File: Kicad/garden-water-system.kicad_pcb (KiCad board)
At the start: 2 copper layers, 75 x 60 mm, 36 parts, among them J1 Conn_01x02, J10 Screw_Terminal_01x05, J11 Conn_01x04, J12 Conn_01x05, J13 Jack-DC, J2 Conn_01x05, J3 Conn_01x03, J4 Conn_01x03, J5 Conn_01x03, J6 Conn_01x03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

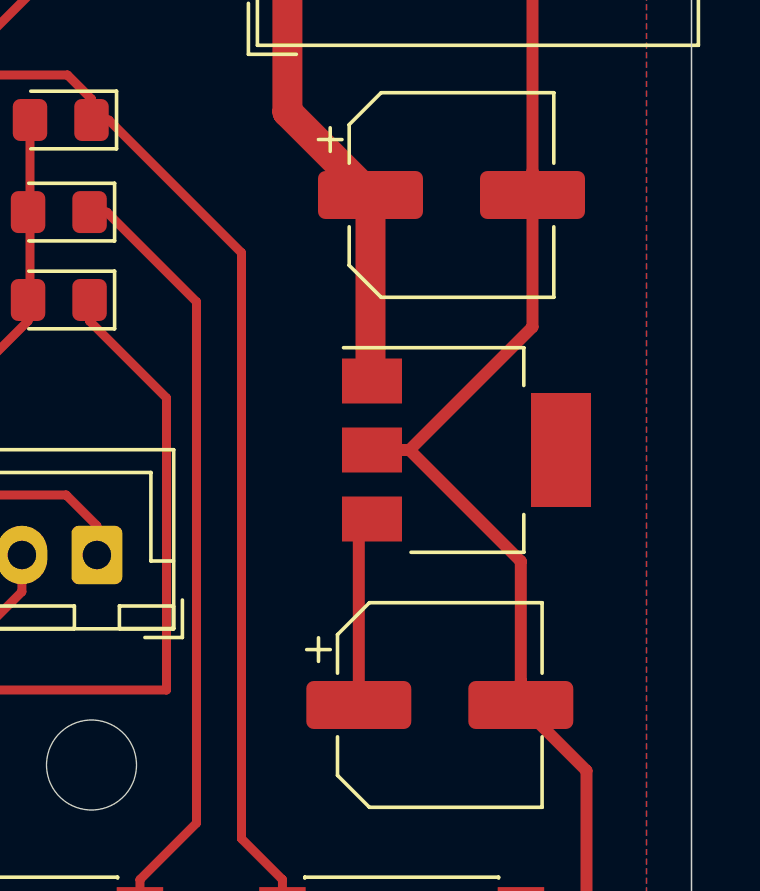
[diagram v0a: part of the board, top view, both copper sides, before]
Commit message: Correction pins AMS1117 5.0
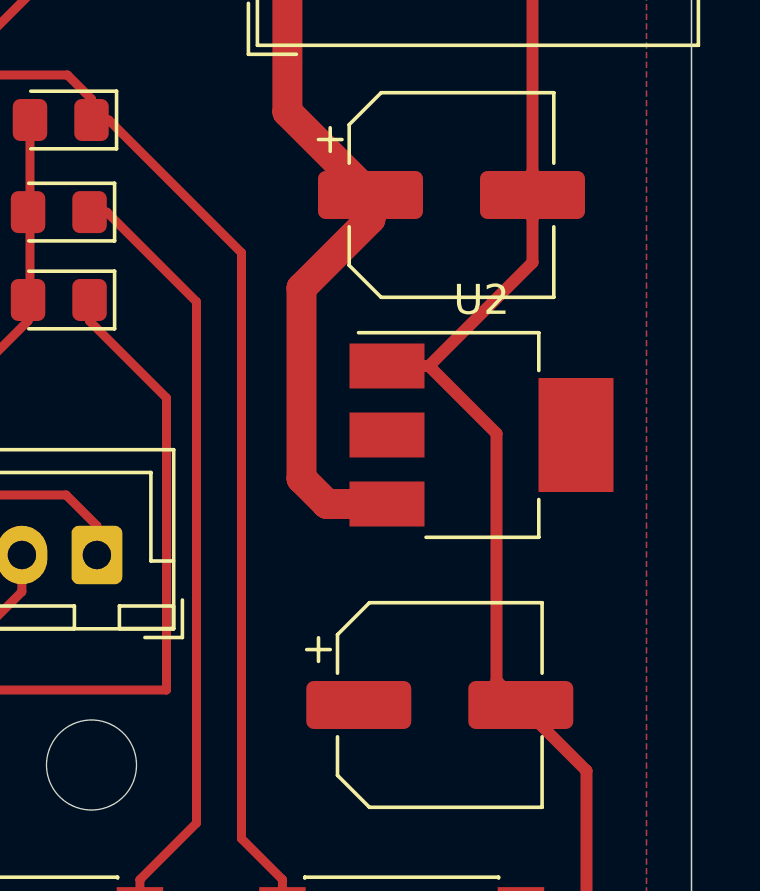
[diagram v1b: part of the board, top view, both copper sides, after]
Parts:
- U2: value LM7805_TO220 -> AMS1117-5.0
- moved U2 0.71 mm to (183.0, 59.5)
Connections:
- U2 pad 1: Net-(C4-Pad1) -> GND
- U2 pad 2: GND -> VCC
- U2 pad 3: VCC -> Net-(C4-Pad1)
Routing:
- net Net-(C4-Pad1): track 23.1 -> 30.5 mm
- net VCC: track 6.38 -> 0.00 mm
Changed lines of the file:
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@@
     (thickness 1.6)
     (drawings 12)
-    (tracks 202)
+    (tracks 204)
     (zones 0)
     (modules 36)
@@
     (mod_text_size 1 1)
     (mod_text_width 0.15)
-    (pad_size 3 3)
-    (pad_drill 3)
+    (pad_size 2.5 3.8)
+    (pad_drill 0)
     (pad_to_mask_clearance 0.051)
     (solder_mask_min_width 0.25)
@@
     (uvia_drill 0.1)
     (add_net VCC)
+  )
+  (module Package_TO_SOT_SMD:SOT-223 (layer F.Cu)
+    (at 183 59.5)
+    (descr "module CMS SOT223 4 pins")
+    (tags "CMS SOT")
+    (attr smd)
+    (fp_text reference U2 (at 0 -4.5) (layer F.SilkS)
+      (effects (font (size 1 1) (thickness 0.15)))
+    )
+    (fp_text value AMS1117-5.0 (at 0 4.5) (layer F.Fab)
+      (effects (font (size 1 1) (thickness 0.15)))
+    )
+    (fp_line (start 1.85 -3.35) (end 1.85 3.35) (layer F.Fab) (width 0.1))
+    (fp_line (start -1.85 3.35) (end 1.85 3.35) (layer F.Fab) (width 0.1))
+    (fp_line (start -4.1 -3.41) (end 1.91 -3.41) (layer F.SilkS) (width 0.12))
+    (fp_line (start -0.8 -3.35) (end 1.85 -3.35) (layer F.Fab) (width 0.1))
+    (fp_line (start -1.85 3.41) (end 1.91 3.41) (layer F.SilkS) (width 0.12))
+    (fp_line (start -1.85 -2.3) (end -1.85 3.35) (layer F.Fab) (width 0.1))
+    (fp_line (start -4.4 -3.6) (end -4.4 3.6) (layer F.CrtYd) (width 0.05))
+    (fp_line (start -4.4 3.6) (end 4.4 3.6) (layer F.CrtYd) (width 0.05))
+    (fp_line (start 4.4 3.6) (end 4.4 -3.6) (layer F.CrtYd) (width 0.05))
+    (fp_line (start 4.4 -3.6) (end -4.4 -3.6) (layer F.CrtYd) (width 0.05))
+    (fp_line (start 1.91 -3.41) (end 1.91 -2.15) (layer F.SilkS) (width 0.12))
+    (fp_line (start 1.91 3.41) (end 1.91 2.15) (layer F.SilkS) (width 0.12))
+    (fp_line (start -1.85 -2.3) (end -0.8 -3.35) (layer F.Fab) (width 0.1))
+    (fp_text user %R (at 0 0 90) (layer F.Fab)
+      (effects (font (size 0.8 0.8) (thickness 0.12)))
+    )
+    (pad 1 smd rect (at -3.15 -2.3) (size 2.5 1.5) (layers F.Cu F.Paste F.Mask)
+      (net 2 GND))
+    (pad 3 smd rect (at -3.15 2.3) (size 2.5 1.5) (layers F.Cu F.Paste F.Mask)
+      (net 5 "Net-(C4-Pad1)"))
+    (pad 2 smd rect (at -3.15 0) (size 2.5 1.5) (layers F.Cu F.Paste F.Mask)
+      (net 4 VCC))
+    (pad 4 smd rect (at 3.15 0) (size 2.5 3.8) (layers F.Cu F.Paste F.Mask))
+    (model ${KISYS3DMOD}/Package_TO_SOT_SMD.3dshapes/SOT-223.wrl
+      (at (xyz 0 0 0))
+      (scale (xyz 1 1 1))
+      (rotate (xyz 0 0 0))
+    )
   )
   (module Diode_SMD:D_2010_5025Metric_Pad1.52x2.65mm_HandSolder (layer F.Cu)
@@
       (xy 1.747822 3.017822)) (layer F.SilkS) (width 0.01))
   )
-  (module Package_TO_SOT_SMD:SOT-223 (layer F.Cu)
-    (at 182.5 60)
-    (descr "module CMS SOT223 4 pins")
-    (tags "CMS SOT")
-    (attr smd)
-    (fp_text reference U2 (at 3.5 -3.5) (layer F.SilkS) hide
-      (effects (font (size 1 1) (thickness 0.15)))
-    )
-    (fp_text value LM7805_TO220 (at 0 4.5) (layer F.Fab)
-      (effects (font (size 1 1) (thickness 0.15)))
-    )
-    (fp_line (start 1.85 -3.35) (end 1.85 3.35) (layer F.Fab) (width 0.1))
-    (fp_line (start -1.85 3.35) (end 1.85 3.35) (layer F.Fab) (width 0.1))
-    (fp_line (start -4.1 -3.41) (end 1.91 -3.41) (layer F.SilkS) (width 0.12))
-    (fp_line (start -0.8 -3.35) (end 1.85 -3.35) (layer F.Fab) (width 0.1))
-    (fp_line (start -1.85 3.41) (end 1.91 3.41) (layer F.SilkS) (width 0.12))
-    (fp_line (start -1.85 -2.3) (end -1.85 3.35) (layer F.Fab) (width 0.1))
-    (fp_line (start -4.4 -3.6) (end -4.4 3.6) (layer F.CrtYd) (width 0.05))
-    (fp_line (start -4.4 3.6) (end 4.4 3.6) (layer F.CrtYd) (width 0.05))
-    (fp_line (start 4.4 3.6) (end 4.4 -3.6) (layer F.CrtYd) (width 0.05))
-    (fp_line (start 4.4 -3.6) (end -4.4 -3.6) (layer F.CrtYd) (width 0.05))
-    (fp_line (start 1.91 -3.41) (end 1.91 -2.15) (layer F.SilkS) (width 0.12))
-    (fp_line (start 1.91 3.41) (end 1.91 2.15) (layer F.SilkS) (width 0.12))
-    (fp_line (start -1.85 -2.3) (end -0.8 -3.35) (layer F.Fab) (width 0.1))
-    (fp_text user %R (at 0 0) (layer F.Fab)
-      (effects (font (size 1 1) (thickness 0.15)))
-    )
-    (pad 1 smd rect (at -3.15 -2.3) (size 2 1.5) (layers F.Cu F.Paste F.Mask)
-      (net 5 "Net-(C4-Pad1)"))
-    (pad 3 smd rect (at -3.15 2.3) (size 2 1.5) (layers F.Cu F.Paste F.Mask)
-      (net 4 VCC))
-    (pad 2 smd rect (at -3.15 0) (size 2 1.5) (layers F.Cu F.Paste F.Mask)
-      (net 2 GND))
-    (pad 4 smd rect (at 3.15 0) (size 2 3.8) (layers F.Cu F.Paste F.Mask))
-    (model ${KISYS3DMOD}/Package_TO_SOT_SMD.3dshapes/SOT-223.wrl
-      (at (xyz 0 0 0))
-      (scale (xyz 1 1 1))
-      (rotate (xyz 0 0 0))
-    )
-  )
   (module Connector_BarrelJack:BarrelJack_Wuerth_6941xx301002 (layer F.Cu)
     (at 176.53 41.91 90)
@@
   (segment (start 183.48 41.91) (end 184.7 43.13) (width 0.4) (layer F.Cu) (net 2))
   (segment (start 182.33 41.91) (end 183.48 41.91) (width 0.4) (layer F.Cu) (net 2))
-  (segment (start 184.7 55.9) (end 180.6 60) (width 0.4) (layer F.Cu) (net 2))
-  (segment (start 184.7 51.5) (end 184.7 55.9) (width 0.4) (layer F.Cu) (net 2))
-  (segment (start 184.31 67.7) (end 184.31 68.5) (width 0.4) (layer F.Cu) (net 2))
-  (segment (start 184.31 63.71) (end 184.31 67.7) (width 0.4) (layer F.Cu) (net 2))
-  (segment (start 180.6 60) (end 184.31 63.71) (width 0.4) (layer F.Cu) (net 2))
-  (segment (start 179.35 60) (end 180.6 60) (width 0.4) (layer F.Cu) (net 2))
   (segment (start 167.4 41) (end 165.9 39.5) (width 0.4) (layer F.Cu) (net 2))
   (segment (start 167.975 41) (end 167.4 41) (width 0.4) (layer F.Cu) (net 2))
@@
   (segment (start 160 39.5) (end 158.75 40.75) (width 0.4) (layer F.Cu) (net 2))
   (segment (start 165.9 39.5) (end 160 39.5) (width 0.4) (layer F.Cu) (net 2))
+  (segment (start 184.7 53.75) (end 184.7 52.3) (width 0.4) (layer F.Cu) (net 2))
+  (segment (start 181.25 57.2) (end 184.7 53.75) (width 0.4) (layer F.Cu) (net 2))
+  (segment (start 184.7 52.3) (end 184.7 51.5) (width 0.4) (layer F.Cu) (net 2))
+  (segment (start 179.85 57.2) (end 181.25 57.2) (width 0.4) (layer F.Cu) (net 2))
+  (segment (start 181.25 57.2) (end 183.5 59.45) (width 0.4) (layer F.Cu) (net 2))
+  (segment (start 183.5 67.69) (end 184.31 68.5) (width 0.4) (layer F.Cu) (net 2))
+  (segment (start 183.5 59.45) (end 183.5 67.69) (width 0.4) (layer F.Cu) (net 2))
   (segment (start 143.51 72.5) (end 143.51 70.01) (width 0.3) (layer F.Cu) (net 3))
   (segment (start 142.24 68.74) (end 142.24 66.04) (width 0.3) (layer F.Cu) (net 3))
@@
   (segment (start 143.51 77) (end 143.51 72.5) (width 0.3) (layer F.Cu) (net 3))
   (segment (start 143.51 77.7) (end 143.51 77) (width 0.3) (layer F.Cu) (net 3))
-  (segment (start 178.91 62.74) (end 179.35 62.3) (width 0.4) (layer F.Cu) (net 4))
-  (segment (start 178.91 68.5) (end 178.91 62.74) (width 0.4) (layer F.Cu) (net 4))
   (segment (start 176.53 48.73) (end 179.3 51.5) (width 1) (layer F.Cu) (net 5))
   (segment (start 176.53 41.91) (end 176.53 48.73) (width 1) (layer F.Cu) (net 5))
-  (segment (start 179.3 57.65) (end 179.35 57.7) (width 1) (layer F.Cu) (net 5))
-  (segment (start 179.3 51.5) (end 179.3 57.65) (width 1) (layer F.Cu) (net 5))
   (segment (start 172.8375 38.2175) (end 176.53 41.91) (width 1) (layer F.Cu) (net 5))
   (segment (start 172.8375 37.25) (end 172.8375 38.2175) (width 1) (layer F.Cu) (net 5))
+  (segment (start 179.3 52.3) (end 177 54.6) (width 1) (layer F.Cu) (net 5))
+  (segment (start 179.3 51.5) (end 179.3 52.3) (width 1) (layer F.Cu) (net 5))
+  (segment (start 177.85 61.8) (end 179.85 61.8) (width 1) (layer F.Cu) (net 5))
+  (segment (start 177 60.95) (end 177.85 61.8) (width 1) (layer F.Cu) (net 5))
+  (segment (start 177 54.6) (end 177 60.95) (width 1) (layer F.Cu) (net 5))
   (segment (start 167.95 54.935) (end 167.885 55) (width 0.3) (layer F.Cu) (net 6))
   (segment (start 167.95 49) (end 167.95 54.935) (width 0.3) (layer F.Cu) (net 6))
